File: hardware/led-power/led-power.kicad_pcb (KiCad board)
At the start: 4 copper layers, 86.4 x 86.4 mm, 88 parts, among them J1 String1, J10 Conn_01x05_Male, J11 Qwiic, J12 Qwiic, J16 I2C Header, J17 IRQ, J2 String2, J3 String3, J4 String4, J5 String5, J6 String6, J7 String7, J8 String8, J9 PowerInput, Q1 Q_NMOS_GDS, Q2 Q_NMOS_GDS, Q3 Q_NMOS_GDS, Q4 Q_NMOS_GDS, Q5 Q_NMOS_GDS, Q6 Q_NMOS_GDS, Q7 Q_NMOS_GDS, Q8 Q_NMOS_GDS, Q9 Q_NPN_BEC, U1 MCP6V51, U10 L78L05ACZ-AP, U11 MCP1501, U12 LM317_TO-220, U2 MCP6V51, U3 MCP6V51, U4 MCP6V51, U5 MCP6V51, U6 MCP6V51, U7 MCP6V51, U8 MCP6V51, U9 STM32G030Fx

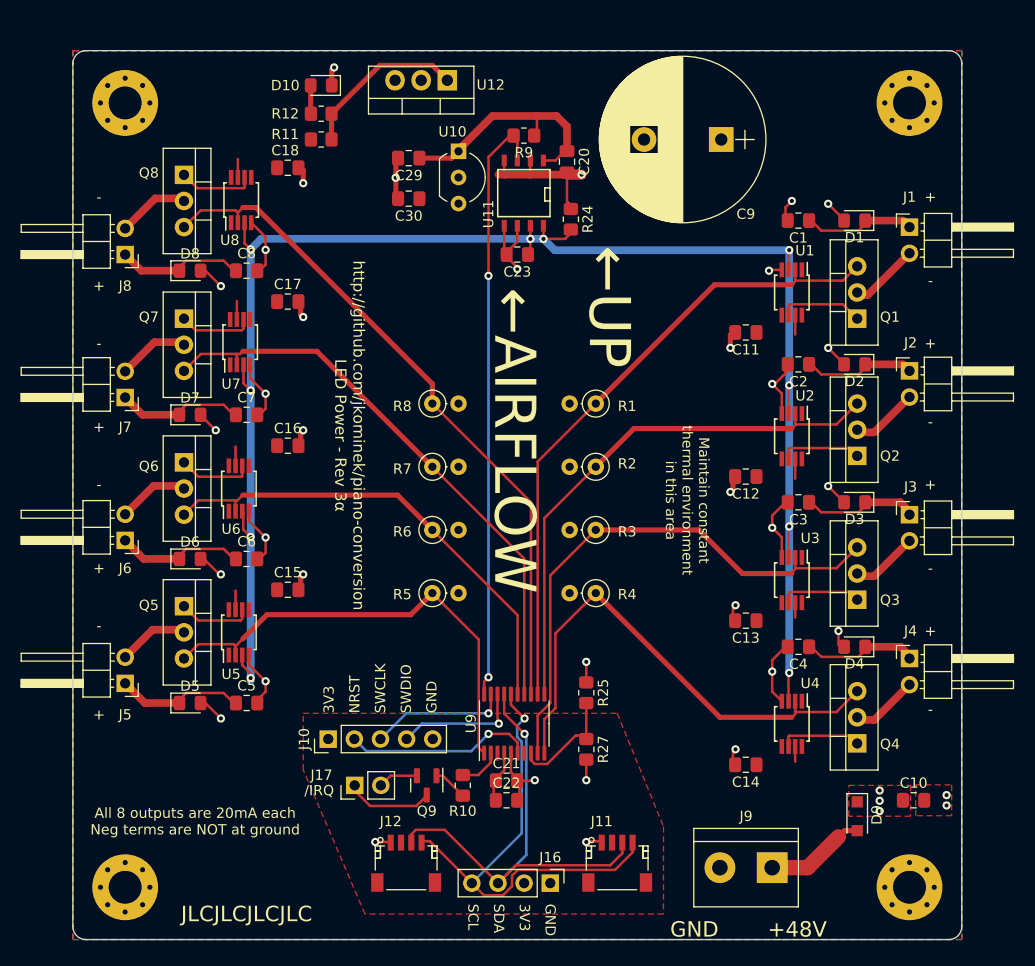
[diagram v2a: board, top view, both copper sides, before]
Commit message: Convert all other mounting holes to non-pad variety.
Reroute a few traces to be shorter.
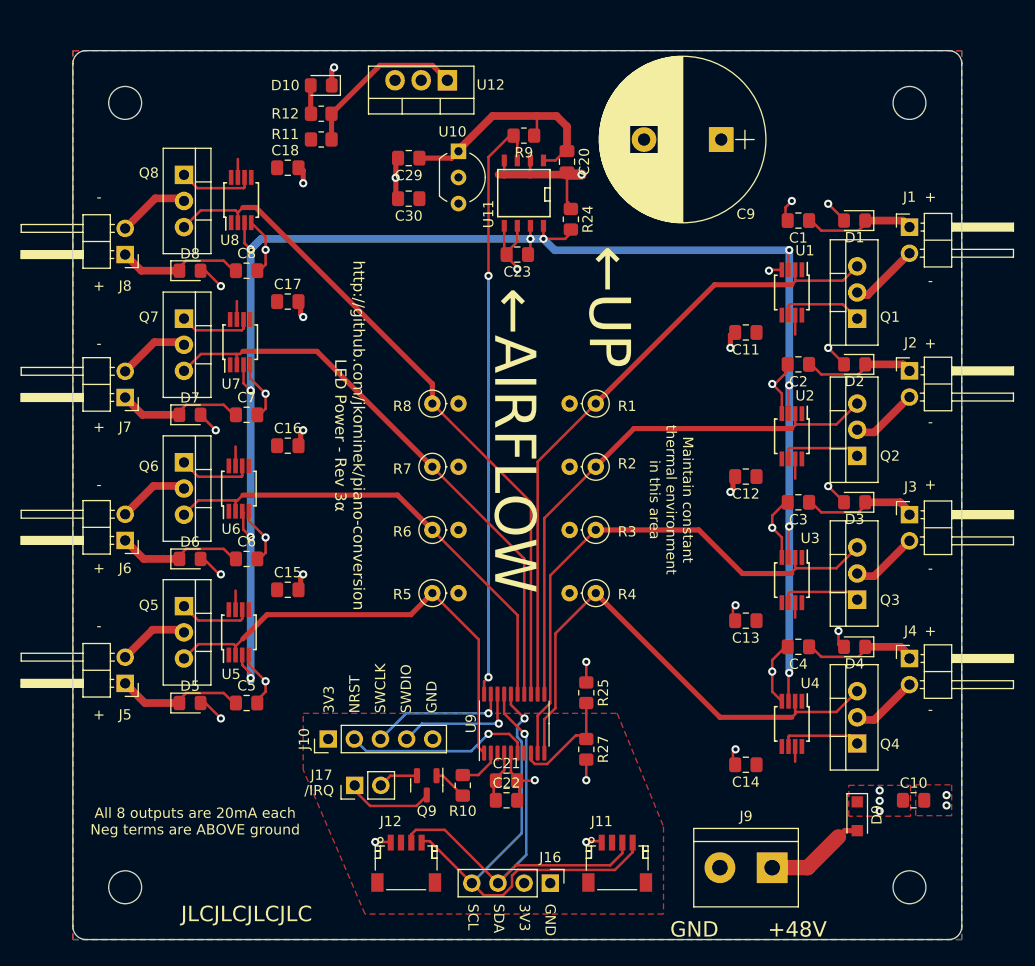
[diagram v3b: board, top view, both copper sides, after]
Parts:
- H1, H2, H3, H4: footprint Mounting_Holes:MountingHole_3.2mm_M3_Pad_Via -> MountingHole:MountingHole_3.2mm_M3
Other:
- board text added: "All 8 outputs are 20mA each Neg terms are ABOVE ground"
- board text removed: "All 8 outputs are 20mA each Neg terms are NOT at ground"
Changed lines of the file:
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@@
       (net 33 "/SCL") (pinfunction "Pin_4") (pintype "passive"))
   )
-  (footprint "Mounting_Holes:MountingHole_3.2mm_M3_Pad_Via" locked (layer "F.Cu")
+  (footprint "MountingHole:MountingHole_3.2mm_M3" locked (layer "F.Cu")
     (at 152.4 76.2)
-    (descr "Mounting Hole 3.2mm, M3")
-    (tags "mounting hole 3.2mm m3")
+    (descr "Mounting Hole 3.2mm, no annular, M3")
+    (tags "mounting hole 3.2mm no annular m3")
     (property "Sheetfile" "led-power.kicad_sch")
     (property "Sheetname" "")
@@
     (fp_circle (center 0 0) (end 3.2 0) (layer "Cmts.User") (width 0.15) (fill none))
     (fp_circle (center 0 0) (end 3.45 0) (layer "F.CrtYd") (width 0.05) (fill none))
-    (pad "1" thru_hole circle locked (at -2.4 0) (size 0.8 0.8) (drill 0.5) (layers *.Cu *.Mask)
-      (net 1 "GND") (pinfunction "1") (pintype "input"))
-    (pad "1" thru_hole circle locked (at 2.4 0) (size 0.8 0.8) (drill 0.5) (layers *.Cu *.Mask)
-      (net 1 "GND") (pinfunction "1") (pintype "input"))
-    (pad "1" thru_hole circle locked (at -1.697056 1.697056) (size 0.8 0.8) (drill 0.5) (layers *.Cu *.Mask)
-      (net 1 "GND") (pinfunction "1") (pintype "input"))
-    (pad "1" thru_hole circle locked (at 0 2.4) (size 0.8 0.8) (drill 0.5) (layers *.Cu *.Mask)
-      (net 1 "GND") (pinfunction "1") (pintype "input"))
-    (pad "1" thru_hole circle locked (at -1.697056 -1.697056) (size 0.8 0.8) (drill 0.5) (layers *.Cu *.Mask)
-      (net 1 "GND") (pinfunction "1") (pintype "input"))
-    (pad "1" thru_hole circle locked (at 1.697056 1.697056) (size 0.8 0.8) (drill 0.5) (layers *.Cu *.Mask)
-      (net 1 "GND") (pinfunction "1") (pintype "input"))
-    (pad "1" thru_hole circle locked (at 0 0) (size 6.4 6.4) (drill 3.2) (layers *.Cu *.Mask)
-      (net 1 "GND") (pinfunction "1") (pintype "input"))
-    (pad "1" thru_hole circle locked (at 0 -2.4) (size 0.8 0.8) (drill 0.5) (layers *.Cu *.Mask)
-      (net 1 "GND") (pinfunction "1") (pintype "input"))
-    (pad "1" thru_hole circle locked (at 1.697056 -1.697056) (size 0.8 0.8) (drill 0.5) (layers *.Cu *.Mask)
-      (net 1 "GND") (pinfunction "1") (pintype "input"))
-  )
-  (footprint "Mounting_Holes:MountingHole_3.2mm_M3_Pad_Via" locked (layer "F.Cu")
+    (pad "" np_thru_hole circle locked (at 0 0) (size 3.2 3.2) (drill 3.2) (layers *.Cu *.Mask))
+  )
+  (footprint "MountingHole:MountingHole_3.2mm_M3" locked (layer "F.Cu")
     (at 152.4 152.4)
-    (descr "Mounting Hole 3.2mm, M3")
-    (tags "mounting hole 3.2mm m3")
+    (descr "Mounting Hole 3.2mm, no annular, M3")
+    (tags "mounting hole 3.2mm no annular m3")
     (property "Sheetfile" "led-power.kicad_sch")
     (property "Sheetname" "")
@@
     (fp_circle (center 0 0) (end 3.2 0) (layer "Cmts.User") (width 0.15) (fill none))
     (fp_circle (center 0 0) (end 3.45 0) (layer "F.CrtYd") (width 0.05) (fill none))
-    (pad "1" thru_hole circle locked (at 0 2.4) (size 0.8 0.8) (drill 0.5) (layers *.Cu *.Mask)
-      (net 1 "GND") (pinfunction "1") (pintype "input"))
-    (pad "1" thru_hole circle locked (at 0 0) (size 6.4 6.4) (drill 3.2) (layers *.Cu *.Mask)
-      (net 1 "GND") (pinfunction "1") (pintype "input"))
-    (pad "1" thru_hole circle locked (at 1.697056 -1.697056) (size 0.8 0.8) (drill 0.5) (layers *.Cu *.Mask)
-      (net 1 "GND") (pinfunction "1") (pintype "input"))
-    (pad "1" thru_hole circle locked (at -1.697056 1.697056) (size 0.8 0.8) (drill 0.5) (layers *.Cu *.Mask)
-      (net 1 "GND") (pinfunction "1") (pintype "input"))
-    (pad "1" thru_hole circle locked (at -2.4 0) (size 0.8 0.8) (drill 0.5) (layers *.Cu *.Mask)
-      (net 1 "GND") (pinfunction "1") (pintype "input"))
-    (pad "1" thru_hole circle locked (at 1.697056 1.697056) (size 0.8 0.8) (drill 0.5) (layers *.Cu *.Mask)
-      (net 1 "GND") (pinfunction "1") (pintype "input"))
-    (pad "1" thru_hole circle locked (at 2.4 0) (size 0.8 0.8) (drill 0.5) (layers *.Cu *.Mask)
-      (net 1 "GND") (pinfunction "1") (pintype "input"))
-    (pad "1" thru_hole circle locked (at 0 -2.4) (size 0.8 0.8) (drill 0.5) (layers *.Cu *.Mask)
-      (net 1 "GND") (pinfunction "1") (pintype "input"))
-    (pad "1" thru_hole circle locked (at -1.697056 -1.697056) (size 0.8 0.8) (drill 0.5) (layers *.Cu *.Mask)
-      (net 1 "GND") (pinfunction "1") (pintype "input"))
-  )
-  (footprint "Mounting_Holes:MountingHole_3.2mm_M3_Pad_Via" locked (layer "F.Cu")
+    (pad "" np_thru_hole circle locked (at 0 0) (size 3.2 3.2) (drill 3.2) (layers *.Cu *.Mask))
+  )
+  (footprint "MountingHole:MountingHole_3.2mm_M3" locked (layer "F.Cu")
     (at 76.2 152.4)
-    (descr "Mounting Hole 3.2mm, M3")
-    (tags "mounting hole 3.2mm m3")
+    (descr "Mounting Hole 3.2mm, no annular, M3")
+    (tags "mounting hole 3.2mm no annular m3")
     (property "Sheetfile" "led-power.kicad_sch")
     (property "Sheetname" "")
@@
     (fp_circle (center 0 0) (end 3.2 0) (layer "Cmts.User") (width 0.15) (fill none))
     (fp_circle (center 0 0) (end 3.45 0) (layer "F.CrtYd") (width 0.05) (fill none))
-    (pad "1" thru_hole circle locked (at 0 0) (size 6.4 6.4) (drill 3.2) (layers *.Cu *.Mask)
-      (net 1 "GND") (pinfunction "1") (pintype "input"))
-    (pad "1" thru_hole circle locked (at 1.697056 -1.697056) (size 0.8 0.8) (drill 0.5) (layers *.Cu *.Mask)
-      (net 1 "GND") (pinfunction "1") (pintype "input"))
-    (pad "1" thru_hole circle locked (at 0 -2.4) (size 0.8 0.8) (drill 0.5) (layers *.Cu *.Mask)
-      (net 1 "GND") (pinfunction "1") (pintype "input"))
-    (pad "1" thru_hole circle locked (at -1.697056 1.697056) (size 0.8 0.8) (drill 0.5) (layers *.Cu *.Mask)
-      (net 1 "GND") (pinfunction "1") (pintype "input"))
-    (pad "1" thru_hole circle locked (at 1.697056 1.697056) (size 0.8 0.8) (drill 0.5) (layers *.Cu *.Mask)
-      (net 1 "GND") (pinfunction "1") (pintype "input"))
-    (pad "1" thru_hole circle locked (at -2.4 0) (size 0.8 0.8) (drill 0.5) (layers *.Cu *.Mask)
-      (net 1 "GND") (pinfunction "1") (pintype "input"))
-    (pad "1" thru_hole circle locked (at -1.697056 -1.697056) (size 0.8 0.8) (drill 0.5) (layers *.Cu *.Mask)
-      (net 1 "GND") (pinfunction "1") (pintype "input"))
-    (pad "1" thru_hole circle locked (at 0 2.4) (size 0.8 0.8) (drill 0.5) (layers *.Cu *.Mask)
-      (net 1 "GND") (pinfunction "1") (pintype "input"))
-    (pad "1" thru_hole circle locked (at 2.4 0) (size 0.8 0.8) (drill 0.5) (layers *.Cu *.Mask)
-      (net 1 "GND") (pinfunction "1") (pintype "input"))
-  )
-  (footprint "Mounting_Holes:MountingHole_3.2mm_M3_Pad_Via" locked (layer "F.Cu")
+    (pad "" np_thru_hole circle locked (at 0 0) (size 3.2 3.2) (drill 3.2) (layers *.Cu *.Mask))
+  )
+  (footprint "MountingHole:MountingHole_3.2mm_M3" locked (layer "F.Cu")
     (at 76.2 76.2)
-    (descr "Mounting Hole 3.2mm, M3")
-    (tags "mounting hole 3.2mm m3")
+    (descr "Mounting Hole 3.2mm, no annular, M3")
+    (tags "mounting hole 3.2mm no annular m3")
     (property "Sheetfile" "led-power.kicad_sch")
     (property "Sheetname" "")
@@
     (fp_circle (center 0 0) (end 3.2 0) (layer "Cmts.User") (width 0.15) (fill none))
     (fp_circle (center 0 0) (end 3.45 0) (layer "F.CrtYd") (width 0.05) (fill none))
-    (pad "1" thru_hole circle locked (at 2.4 0) (size 0.8 0.8) (drill 0.5) (layers *.Cu *.Mask)
-      (net 1 "GND") (pinfunction "1") (pintype "input"))
-    (pad "1" thru_hole circle locked (at 1.697056 1.697056) (size 0.8 0.8) (drill 0.5) (layers *.Cu *.Mask)
-      (net 1 "GND") (pinfunction "1") (pintype "input"))
-    (pad "1" thru_hole circle locked (at 0 0) (size 6.4 6.4) (drill 3.2) (layers *.Cu *.Mask)
-      (net 1 "GND") (pinfunction "1") (pintype "input"))
-    (pad "1" thru_hole circle locked (at -1.697056 1.697056) (size 0.8 0.8) (drill 0.5) (layers *.Cu *.Mask)
-      (net 1 "GND") (pinfunction "1") (pintype "input"))
-    (pad "1" thru_hole circle locked (at -1.697056 -1.697056) (size 0.8 0.8) (drill 0.5) (layers *.Cu *.Mask)
-      (net 1 "GND") (pinfunction "1") (pintype "input"))
-    (pad "1" thru_hole circle locked (at 1.697056 -1.697056) (size 0.8 0.8) (drill 0.5) (layers *.Cu *.Mask)
-      (net 1 "GND") (pinfunction "1") (pintype "input"))
-    (pad "1" thru_hole circle locked (at 0 -2.4) (size 0.8 0.8) (drill 0.5) (layers *.Cu *.Mask)
-      (net 1 "GND") (pinfunction "1") (pintype "input"))
-    (pad "1" thru_hole circle locked (at -2.4 0) (size 0.8 0.8) (drill 0.5) (layers *.Cu *.Mask)
-      (net 1 "GND") (pinfunction "1") (pintype "input"))
-    (pad "1" thru_hole circle locked (at 0 2.4) (size 0.8 0.8) (drill 0.5) (layers *.Cu *.Mask)
-      (net 1 "GND") (pinfunction "1") (pintype "input"))
+    (pad "" np_thru_hole circle locked (at 0 0) (size 3.2 3.2) (drill 3.2) (layers *.Cu *.Mask))
   )
   (footprint "Pin_Headers:Pin_Header_Straight_1x04_Pitch2.54mm" (layer "F.Cu")
@@
     (effects (font (size 1 1) (thickness 0.15)) (justify left))
   )
-  (gr_text "All 8 outputs are 20mA each\nNeg terms are NOT at ground" (at 83 146) (layer "F.SilkS")
+  (gr_text "All 8 outputs are 20mA each\nNeg terms are ABOVE ground" (at 83 146) (layer "F.SilkS")
     (effects (font (size 1 1) (thickness 0.15)))
   )
@@
     (effects (font (size 1 1) (thickness 0.15)) (justify left))
   )
-  (gr_text "Maintain constant\nthermal environment\nin this area" (at 130.81 114.808 270) (layer "F.SilkS")
+  (gr_text "Maintain constant\nthermal environment\nin this area" (at 129.25 114.75 270) (layer "F.SilkS")
     (effects (font (size 1 1) (thickness 0.15)))
   )
@@
   )
   (zone (net 46) (net_name "+12V") (layer "F.Cu") (hatch edge 0.508)
-    (connect_pads (clearance 0.508))
-    (min_thickness 0.254) (filled_areas_thickness no)
+    (connect_pads (clearance 0.5))
+    (min_thickness 0.25) (filled_areas_thickness no)
     (fill yes (thermal_gap 0.5) (thermal_bridge_width 0.35))
     (polygon
